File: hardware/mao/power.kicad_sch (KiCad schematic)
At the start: 36 parts, among them J101 USB-C, J102 BAT, Q101 AO3401A, U101 TPD2E2U06, U102 BQ24073RGTR, U103 MAX17048G+T10, U104 TPS63802DLAR, U105 TPS22917DBVR

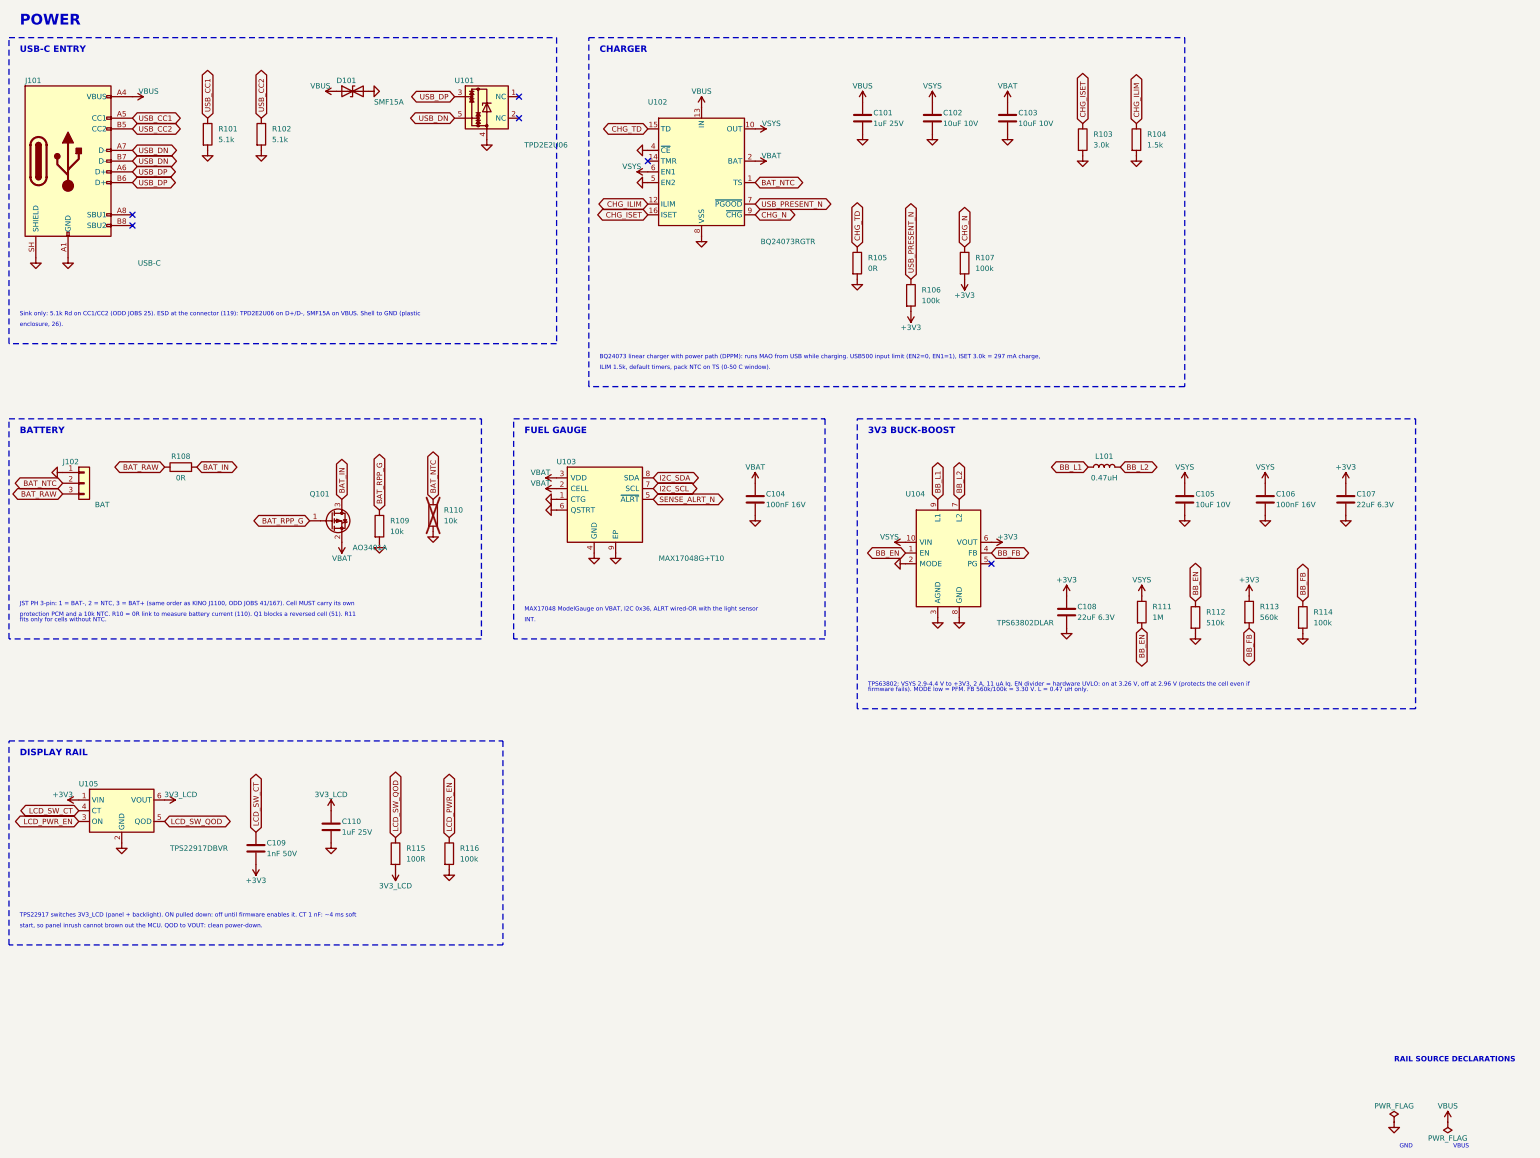
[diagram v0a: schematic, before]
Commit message: hardware: MAO_MAIN A0 routed board, fab package and final review
6-layer JLC06161H-3313 board (F / GND / signals / +3V3 / GND / B), routed from the
design scripts: designed power and fan-out copper, grid router with closed-set A*,
stub pruning, GND stitching (two ties on large pour fragments), tidy.
DRC 0 violations / 0 unconnected / 0 parity; ERC 0; silkscreen checker 0 findings.

- silkscreen: ODD JOBS mark and identity on both faces, S/N box, function-named
  test pads in a 3.0 x 3.2 mm service field; references for every semiconductor and
  connector plus the passives the service docs name, the rest on assembly drawings
- stackup, black mask, white legend and ENIG written into the board
- fab: 6-layer Gerbers + drill, JLC BOM (47 lines, LCSC on every line) and CPL
  (113 parts), assembly PDFs, FAB-NOTES with computed via counts
- docs: PCB, ODD JOBS and order-readiness review sections, final report, renders,
  factory-test pad map, bring-up and architecture updates

Co-Authored-By: Claude Opus 5.5 <noreply@anthropic.com>
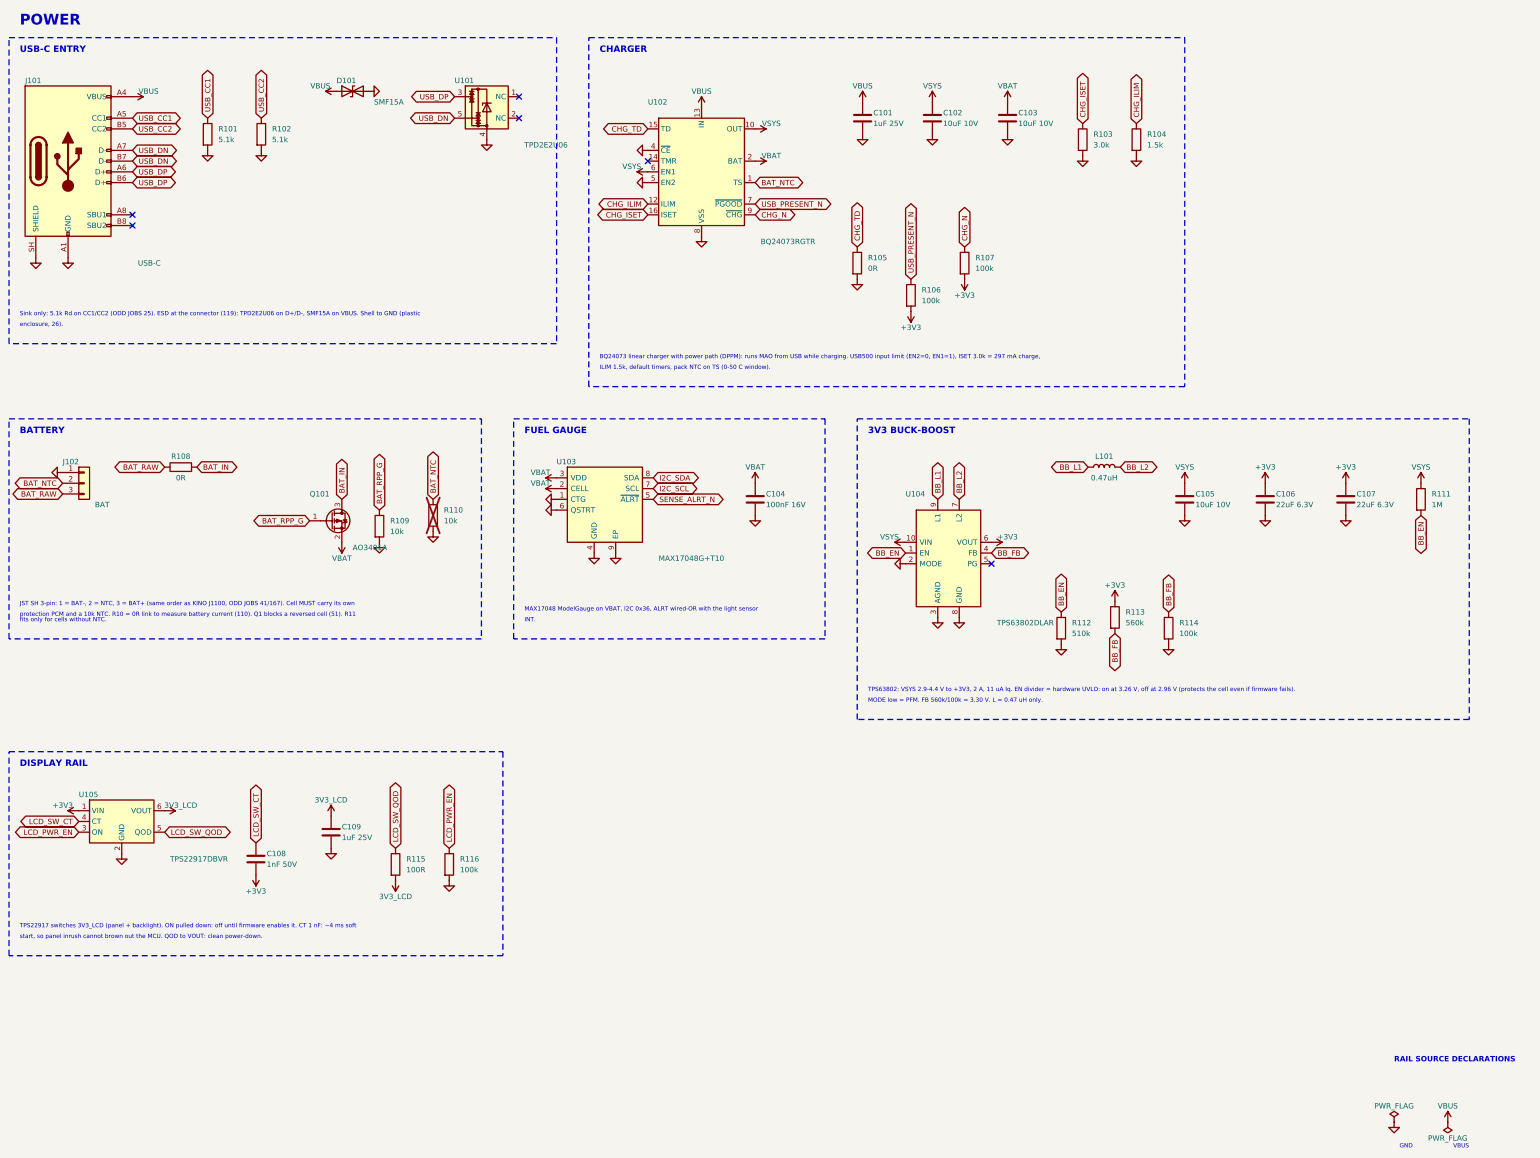
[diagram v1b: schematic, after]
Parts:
- removed C110: 1uF 25V, Capacitor_SMD:C_0402_1005Metric, symbol Device:C
- C106: value 100nF 16V -> 22uF 6.3V; footprint Capacitor_SMD:C_0402_1005Metric -> Capacitor_SMD:C_0603_1608Metric; LCSC C1525 -> C59461; MPN CL05B104KO5NNNC -> CL10A226MQ8NRNC
- C108: value 22uF 6.3V -> 1nF 50V; footprint Capacitor_SMD:C_0603_1608Metric -> Capacitor_SMD:C_0402_1005Metric; LCSC C59461 -> C1523; MPN CL10A226MQ8NRNC -> 0402B102K500NT; Manufacturer Samsung -> FH
- C109: value 1nF 50V -> 1uF 25V; LCSC (none) -> C52923; MPN GRM155R71H102KA01D -> CL05A105KA5NQNC; Manufacturer Murata -> Samsung
- J102: footprint Connector_JST:JST_PH_S3B-PH-SM4-TB_1x03-1MP_P2.00mm_Horizontal -> Connector_JST:JST_SH_SM03B-SRSS-TB_1x03-1MP_P1.00mm_Horizontal; LCSC C265101 -> C7430445; MPN S3B-PH-SM4-TB -> ZX-SH1.0-3PWT (JST SM03B-SRSS-TB compatible); Manufacturer JST -> Megastar
- R108: LCSC (none) -> C17888; MPN RC1206JR-070RL -> 1206W4F0000T5E; Manufacturer YAGEO -> UNI-ROYAL
- R115: LCSC (none) -> C25076; MPN (none) -> 0402WGF1000TCE; Manufacturer (none) -> UNI-ROYAL
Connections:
- net +3V3: now also C106.1, C108.2; no longer C108.1, C109.2
- net 3V3_LCD: now also C109.1
- net GND: now also C109.2; no longer C108.2
- net LCD_SW_CT: now also C108.1; no longer C109.1
- net VSYS: no longer C106.1
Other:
- note added: "JST SH 3-pin: 1 = BAT-, 2 = NTC, 3 = BAT+ (same order as KINO J1100, ODD JOBS 41/167). Cell MUST carry its own"
- note added: "MODE low = PFM. FB 560k/100k = 3.30 V. L = 0.47 uH only."
- note added: "TPS63802: VSYS 2.9-4.4 V to +3V3, 2 A, 11 uA Iq. EN divider = hardware UVLO: on at 3.26 V, off at 2.96 V (protects the cell even if firmware fails)."
- note removed: "JST PH 3-pin: 1 = BAT-, 2 = NTC, 3 = BAT+ (same order as KINO J1100, ODD JOBS 41/167). Cell MUST carry its own"
- note removed: "TPS63802: VSYS 2.9-4.4 V to +3V3, 2 A, 11 uA Iq. EN divider = hardware UVLO: on at 3.26 V, off at 2.96 V (protects the cell even if"
- note removed: "firmware fails). MODE low = PFM. FB 560k/100k = 3.30 V. L = 0.47 uH only."
- moved on the sheet: C108, C109, R111, R112, R113, R114, R115, R116, U105

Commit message: MAO A0: circuit simulation suite and the value fixes it found
- hardware/mao/sim: ngspice (KiCad libngspice) + Python suite S1-S15 with
  plots in docs/hardware/sim and results in mao-a0-verification.md
- UVLO divider 470k/240k (was 1M/510k): EN leakage put the worst-case
  cut-off at 2.65 V; now 2.75-3.16 V
- IR LED resistors 56R (was 47R): peaks were 66-70 mA on USB against the
  65 mA rating; now <= 59 mA
- Firmware: 100 % brightness = 80 % backlight PWM, so the 2.8 V panel bin
  averages <= 40 mA
- Docs: speaker power 0.54 W (was quoted as 0.4 W), UVLO, IR, budget,
  bring-up checks for the backlight bin and the ring strip field
- Capture reports fitted and DNP parts separately

Co-Authored-By: Claude Opus 5.5 <noreply@anthropic.com>
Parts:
- R111: value 1M -> 470k; LCSC C26083 -> C25790; MPN 0402WGF1004TCE -> 0402WGF4703TCE
- R112: value 510k -> 240k; LCSC C11616 -> C64043; MPN 0402WGF5103TCE -> 0402WGF2403TCE
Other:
- note added: "TPS63802: VSYS 2.9-4.4 V to +3V3, 2 A, 11 uA Iq. EN divider = hardware UVLO: on at 3.25 V, off at 2.96 V (protects the cell even if firmware fails)."
- note removed: "TPS63802: VSYS 2.9-4.4 V to +3V3, 2 A, 11 uA Iq. EN divider = hardware UVLO: on at 3.26 V, off at 2.96 V (protects the cell even if firmware fails)."
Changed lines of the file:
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@@
 		)
 	)
-	(text "TPS63802: VSYS 2.9-4.4 V to +3V3, 2 A, 11 uA Iq. EN divider = hardware UVLO: on at 3.26 V, off at 2.96 V (protects the cell even if firmware fails)."
+	(text "TPS63802: VSYS 2.9-4.4 V to +3V3, 2 A, 11 uA Iq. EN divider = hardware UVLO: on at 3.25 V, off at 2.96 V (protects the cell even if firmware fails)."
 		(exclude_from_sim no)
 		(at 215.9 175.26 0)
@@
 			)
 		)
-		(property "Value" "1M"
+		(property "Value" "470k"
 			(at 349.25 130.81 0)
 			(effects
@@
 			)
 		)
-		(property "Description" "UVLO divider top"
+		(property "Description" "UVLO divider top (470k, not 1M: the 0.2 uA EN leakage moves the trip only +/-0.1 V)"
 			(at 346.71 129.54 0)
 			(effects
@@
 			)
 		)
-		(property "MPN" "0402WGF1004TCE"
+		(property "MPN" "0402WGF4703TCE"
 			(at 346.71 129.54 0)
 			(effects
@@
 			)
 		)
-		(property "LCSC" "C26083"
+		(property "LCSC" "C25790"
 			(at 346.71 129.54 0)
 			(effects
@@
 			)
 		)
-		(property "Value" "510k"
+		(property "Value" "240k"
 			(at 264.16 161.29 0)
 			(effects
@@
 			)
 		)
-		(property "MPN" "0402WGF5103TCE"
+		(property "MPN" "0402WGF2403TCE"
 			(at 261.62 160.02 0)
 			(effects
@@
 			)
 		)
-		(property "LCSC" "C11616"
+		(property "LCSC" "C64043"
 			(at 261.62 160.02 0)
 			(effects

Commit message: MAO A0 revision: stock Winstar panel through a tail slot, AW9364 backlight, routed 4-layer board
Hardware changes from the verification audits:
- display: stock Winstar WF0128BTYAA4DNN0 (70 mm tail) through a routed slot at 9 o'clock
  to J301 on B.Cu; panel pin k on pad 19-k
- backlight: VLED+ on VSYS into an AW9364 (U303) constant-current sink, 40 mA nominal;
  Q301/R303-R305 removed
- display rail: TPS22919 (SC70-6, 1.1 mm: fits under the panel) with its VIN cap; CT cap gone
- +3V3 at 3.18 V (FB 536k), UVLO filter cap, charger ISET 4.3k (207 mA), /CE from the
  expander with a pull-down, charger moved to F under the panel, SD_MODE series 2.2k
- IR_TX on GPIO38, EXP_RST_N on GPIO39 (MTCK reset pull-up lit the IR LEDs)
- IR receiver and ToF pulled inside the ring lip; M2 boss / screw-head keep-outs

Layout: re-placed and re-routed. DRC 0 violations, 0 unconnected; every plane one piece
(the grid router now undoes any L3 route or via that splits a plane); 192 through vias.
Silk: type scale, 6 x 6 S/N field with the JLC order-number placeholder, 4.6 mm back mark,
references kept off vias, and a few easter eggs (a sleeping cat under the face, boop,
meow, 9 lives, MADE FOR BAD IDEAS).

Checks: ERC 0, silk text 0 findings, enclosure check 0 findings (mech_check.py), all
simulations pass (S3 AW9364, S10 TPS22919, S13 207 mA). Docs: bring-up, factory test,
power budget, architecture, mechanical (tail path), pin map. Firmware: dev command
"mao power charge off|on", self-test pad floor for the 3.18 V rail; merge patch regenerated.

Co-Authored-By: Claude Opus 5.5 <noreply@anthropic.com>
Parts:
- removed C108: 1nF 50V, Capacitor_SMD:C_0402_1005Metric, symbol Device:C
- removed R107: 100k, Resistor_SMD:R_0402_1005Metric, symbol Device:R
- added C110: 1uF 25V, Capacitor_SMD:C_0402_1005Metric, symbol Device:C
- added C111: 100nF 16V, Capacitor_SMD:C_0402_1005Metric, symbol Device:C
- added R117: 100k, Resistor_SMD:R_0402_1005Metric, symbol Device:R
- R103: value 3.0k -> 4.3k; LCSC C25784 -> C25899; MPN 0402WGF3001TCE -> 0402WGF4301TCE
- R113: value 560k -> 536k; LCSC C132339 -> C68457; MPN 0402WGF5603TCE -> 0402WGF5363TCE
- U105: value TPS22917DBVR -> TPS22919DCKR; footprint Package_TO_SOT_SMD:SOT-23-6 -> Package_TO_SOT_SMD:SOT-363_SC-70-6; symbol Power_Management:TPS22917DBV -> Power_Management:TPS22919DCK; LCSC C2681320 -> C2149796; MPN TPS22917DBVR -> TPS22919DCKR
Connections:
- net +3V3: now also U102.6 (EN1), C110.1
- net BB_EN: now also C111.1
- net GND: now also C110.2, C111.2, R117.2; no longer U102.4 (~{CE})
- net VSYS: no longer U102.6 (EN1)
- net CHG_N: no longer names the net of U102.9 (~{CHG})
- net LCD_SW_CT: no longer names the net of U105.4 (NC)
- new net CHG_CE_N: R117.1, U102.4 (~{CE})
- no-connect marks 6 -> 8
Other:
- note added: "(DPPM): runs MAO from USB while"
- note added: "(cell maximum 250 mA = 0.5C), ILIM 1.5k,"
- note added: "(cell maximum 250 mA = 0.5C), ILIM 1.5k, default timers. Pack NTC on TS: the charger stops outside 0-50 C; the cell allows 0-45 C, so firmware"
- note added: "100 nF so load steps cannot trip it. MODE low = PFM. FB 536k/100k = 3.18 V (3.10-3.28 V worst case: under the panel VCI 3.3 V maximum). L = 0.47 uH"
- note added: "11 uA Iq. EN divider = hardware UVLO: on"
- note added: "43 C board temperature; charging state"
- note added: "BQ24073 linear charger with power path"
- note added: "BQ24073 linear charger with power path (DPPM): runs MAO from USB while charging. USB500 input limit (EN2=0, EN1=+3V3), ISET 4.3k = 207 mA charge"
- note added: "EN1=+3V3), ISET 4.3k = 207 mA charge"
- note added: "Fixed 1.6 ms soft start (datasheet 1.75 ms at 3.6 V), so the ~20 mA panel inrush cannot brown out the MCU. QOD to VOUT"
- note added: "PFM. FB 536k/100k = 3.18 V (3.10-3.28 V"
- note added: "TPS22919 switches 3V3_LCD (panel logic; the backlight runs from VSYS). ON pulled down: off until firmware enables it."
- note added: "TPS63802: VSYS 2.9-4.4 V to +3V3, 2 A,"
- note added: "TPS63802: VSYS 2.9-4.4 V to +3V3, 2 A, 11 uA Iq. EN divider = hardware UVLO: on at 3.25 V, off at 2.96 V (protects the cell even if firmware fails),"
- note added: "allows 0-45 C, so firmware pauses"
- note added: "at 3.25 V, off at 2.96 V (protects the"
- note added: "cell even if firmware fails), 100 nF so"
- note added: "charger stops outside 0-50 C; the cell"
- note added: "charging through /CE (expander P6) above"
- note added: "charging. USB500 input limit (EN2=0,"
- note added: "comes from the gauge (CRATE) and PGOOD,"
- note added: "default timers. Pack NTC on TS: the"
- note added: "load steps cannot trip it. MODE low ="
- note added: "maximum). L = 0.47 uH only."
- note added: "only."
- note added: "panel: its heat stays off the cell."
- note added: "pauses charging through /CE (expander P6) above 43 C board temperature; charging state comes from the gauge (CRATE) and PGOOD, so /CHG is not"
- note added: "protection PCM and a 10k NTC. R108 = 0R link to measure battery current (110). Q101 blocks a reversed cell (51);"
- note added: "so /CHG is not used. On F under the"
- note added: "through 100R: clean power-down. SC70-6, 1.1 mm: it sits under the panel (zone A <= 1.2 mm)."
- note added: "used. On F under the panel: its heat stays off the cell."
- note added: "with USB in, the charger stays in its 4-11 mA short probe. R110 fits only for cells without NTC."
- note added: "worst case: under the panel VCI 3.3 V"
- note removed: "BQ24073 linear charger with power path (DPPM): runs MAO from USB while charging. USB500 input limit (EN2=0, EN1=1), ISET 3.0k = 297 mA charge,"
- note removed: "ILIM 1.5k, default timers, pack NTC on TS (0-50 C window)."
- note removed: "MODE low = PFM. FB 560k/100k = 3.30 V. L = 0.47 uH only."
- note removed: "TPS22917 switches 3V3_LCD (panel + backlight). ON pulled down: off until firmware enables it. CT 1 nF: ~4 ms soft"
- note removed: "TPS63802: VSYS 2.9-4.4 V to +3V3, 2 A, 11 uA Iq. EN divider = hardware UVLO: on at 3.25 V, off at 2.96 V (protects the cell even if firmware fails)."
- note removed: "fits only for cells without NTC."
- note removed: "protection PCM and a 10k NTC. R10 = 0R link to measure battery current (110). Q1 blocks a reversed cell (51). R11"
- note removed: "start, so panel inrush cannot brown out the MCU. QOD to VOUT: clean power-down."
- moved on the sheet: C104, C105, C106, C107, C109, J102, L101, Q101, R108, R109, R110, R111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
